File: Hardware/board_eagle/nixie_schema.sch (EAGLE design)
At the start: 116 parts, among them J2 RTC_CONSMD, J4 RTC_CONTHT, P1 100k, P2 10k, Q1 BC856B, Q3 BC856B, Q4 BCX70H, Q5 NTF5P03, T1 PHOTO_TRANS, U2 MC7940N, U3 1V5, Y1 ECS-.327-7-34B

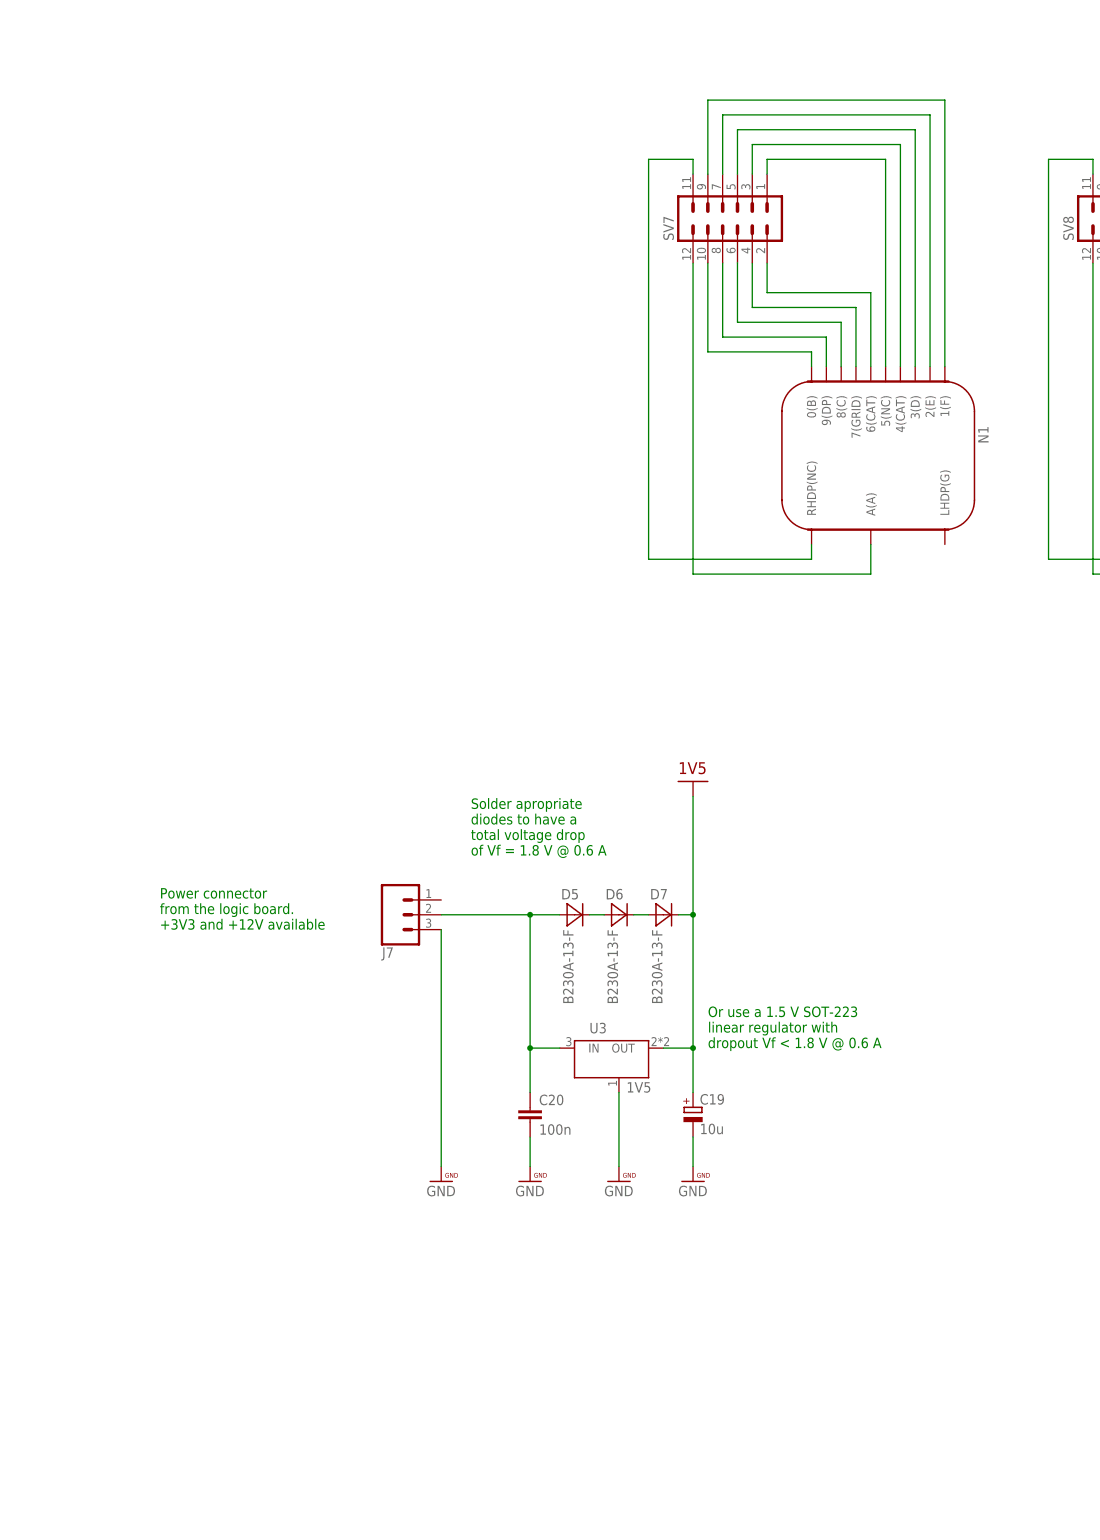
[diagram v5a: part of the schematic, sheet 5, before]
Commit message: Figured out how to wire up tubes to support both IN-14 and IV-11
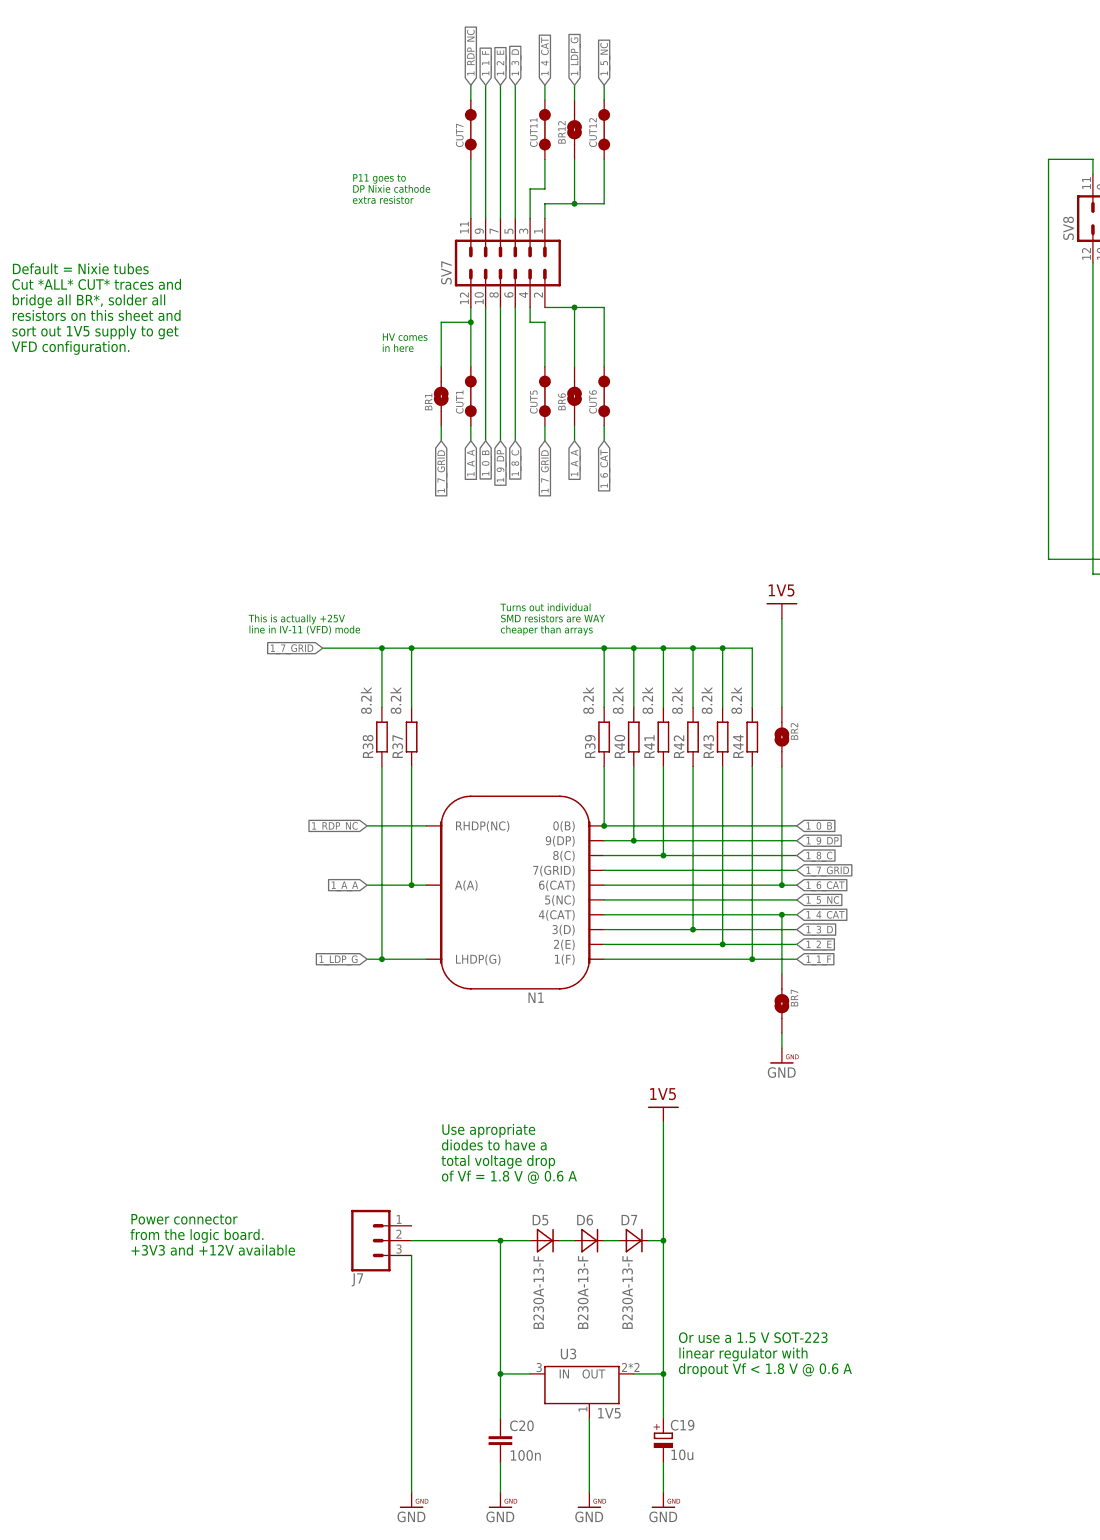
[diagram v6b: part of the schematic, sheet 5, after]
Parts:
- added BR1, BR12, BR2, BR6, BR7: HV_SOLDER_BRIDGE, nixe_cmp:HV_SOLDER_BRIDGE
- added CUT1, CUT11, CUT12, CUT5, CUT6, CUT7: CUT_TRACE, nixe_cmp:CUT_TRACE
- added R37, R38, R39, R40, R41, R42, R43, R44: 8.2k, rcl:R-EU_R0603
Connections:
- removed net N$25: N1.1(F), SV7.9
- removed net N$27: N1.3(D), SV7.5
- removed net N$28: N1.4(CAT), SV7.3
- removed net N$6: N1.7(GRID), SV7.4
- removed net N$7: N1.8(C), SV7.6
- removed net N$94: N1.0(B), SV7.10
- new net 1_0_B: N1.0(B), R39.1, SV7.10
- new net 1_1_F: N1.1(F), R44.1, SV7.9
- new net 1_2_E: N1.2(E), R43.1, SV7.7
- new net 1_3_D: N1.3(D), R42.1, SV7.5
- new net 1_4_CAT: BR7.1, CUT11.2, N1.4(CAT)
- new net 1_5_NC: CUT12.2, N1.5(NC)
- new net 1_6_CAT: CUT6.1, N1.6(CAT)
- new net 1_7_GRID: BR1.1, CUT5.1, N1.7(GRID), R37.2, R38.2, R39.2, R40.2, R41.2, R42.2, R43.2, R44.2
- new net 1_8_C: N1.8(C), R41.1, SV7.6
- new net 1_9_DP: N1.9(DP), R40.1, SV7.8
- new net 1_A_A: BR6.1, CUT1.1, N1.A(A), R37.1
- new net 1_LDP_G: BR12.2, N1.LHDP(G), R38.1
- new net 1_RDP_NC: CUT7.2, N1.RHDP(NC)
- net GND: now also BR7.2
- net N$10: now also BR6.2, CUT6.2, SV7.2; no longer N1.A(A), SV7.12
- net N$2: now also BR1.2, CUT1.2, SV7.12; no longer N1.6(CAT), SV7.2
- net N$24: now also CUT5.2, SV7.4; no longer N1.9(DP), SV7.8
- net N$26: now also CUT7.1, SV7.11; no longer N1.2(E), SV7.7
- net N$29: now also BR12.1, CUT12.1; no longer N1.5(NC)
- net N$30: now also CUT11.1, SV7.3; no longer N1.RHDP(NC), SV7.11
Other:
- note added: "Default = Nixie tubes Cut *ALL* CUT* traces and bridge all BR*, solder all resistors on this sheet and sort out 1V5 supply to get VFD configuration."
- note added: "HV comes in here"
- note added: "P11 goes to DP Nixie cathode extra resistor"
- note added: "This is actually +25V line in IV-11 (VFD) mode"
- note added: "Turns out individual SMD resistors are WAY cheaper than arrays"
- note added: "Use apropriate diodes to have a total voltage drop of Vf = 1.8 V @ 0.6 A"
- note removed: "Solder apropriate diodes to have a total voltage drop of Vf = 1.8 V @ 0.6 A"
- moved on the sheet: C19, C20, D5, D6, D7, J7, N1, SV7, U3

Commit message: Finished tube schematic layout
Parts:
- added BR10, BR11, BR13, BR14, BR15, BR16, BR17, BR18, BR19, BR20, BR21, BR22, BR23, BR24, BR25, BR26, BR27, BR28, BR29, BR3, BR30, BR4, BR5, BR8, BR9: HV_SOLDER_BRIDGE, nixe_cmp:HV_SOLDER_BRIDGE
- added CUT10, CUT13, CUT14, CUT15, CUT16, CUT17, CUT18, CUT19, CUT2, CUT20, CUT21, CUT22, CUT23, CUT24, CUT25, CUT26, CUT27, CUT28, CUT29, CUT3, CUT30, CUT31, CUT32, CUT33, CUT34, CUT35, CUT36, CUT4, CUT8, CUT9: CUT_TRACE, nixe_cmp:CUT_TRACE
- added R45, R46, R47, R48, R49, R50, R51, R52, R53, R54, R55, R56, R57, R58, R59, R60, R61, R62, R63, R64, R65, R66, R67, R68, R69, R70, R71, R72, R73, R74, R75, R76, R77, R78, R79, R80, R81, R82, R83, R84: 8.2k, rcl:R-EU_R0603
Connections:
- removed net N$52: N3.2(E), SV9.7
- removed net N$53: N3.1(F), SV9.9
- removed net N$54: N4.7(GRID), SV10.4
- removed net N$55: N4.8(C), SV10.6
- removed net N$56: N4.9(DP), SV10.8
- removed net N$57: N4.0(B), SV10.10
- removed net N$58: N5.RHDP(NC), SV11.11
- removed net N$59: N4.5(NC), SV10.1
- removed net N$60: N4.4(CAT), SV10.3
- removed net N$61: N4.3(D), SV10.5
- removed net N$62: N4.2(E), SV10.7
- removed net N$63: N4.1(F), SV10.9
- removed net N$64: N5.6(CAT), SV11.2
- removed net N$65: N5.7(GRID), SV11.4
- removed net N$66: N5.8(C), SV11.6
- removed net N$67: N5.9(DP), SV11.8
- removed net N$68: N5.0(B), SV11.10
- removed net N$69: N5.5(NC), SV11.1
- removed net N$70: N5.4(CAT), SV11.3
- removed net N$71: N5.3(D), SV11.5
- removed net N$72: N5.2(E), SV11.7
- removed net N$73: N5.1(F), SV11.9
- removed net N$75: N6.RHDP(NC), SV12.11
- removed net N$76: N6.6(CAT), SV12.2
- removed net N$77: N6.7(GRID), SV12.4
- removed net N$78: N6.8(C), SV12.6
- removed net N$79: N6.9(DP), SV12.8
- removed net N$80: N6.5(NC), SV12.1
- removed net N$81: N6.4(CAT), SV12.3
- removed net N$82: N6.3(D), SV12.5
- removed net N$83: N6.2(E), SV12.7
- removed net N$84: N6.1(F), SV12.9
- removed net N$86: N6.0(B), SV12.10
- removed net N$88: N4.A(A), SV10.12
- removed net N$98: N5.A(A), SV11.12
- new net 2_0_B: N2.0(B), R47.1, SV8.10
- new net 2_1_F: N2.1(F), R52.1, SV8.9
- new net 2_2_E: N2.2(E), R51.1, SV8.7
- new net 2_3_D: N2.3(D), R50.1, SV8.5
- new net 2_4_CAT: BR3.1, CUT9.2, N2.4(CAT)
- new net 2_5_NC: CUT10.2, N2.5(NC)
- new net 2_6_CAT: BR4.2, CUT4.1, N2.6(CAT)
- new net 2_7_GRID: BR5.1, CUT3.1, N2.7(GRID), R45.2, R46.2, R47.2, R48.2, R49.2, R50.2, R51.2, R52.2
- new net 2_8_C: N2.8(C), R49.1, SV8.6
- new net 2_9_DP: N2.9(DP), R48.1, SV8.8
- new net 2_A_A: BR8.1, CUT2.1, N2.A(A), R45.1
- new net 2_LDP_G: BR9.2, N2.LHDP(G), R46.1
- new net 2_RDP_NC: CUT8.2, N2.RHDP(NC)
- new net 3_0_B: N3.0(B), R55.1, SV9.10
- new net 3_1_F: N3.1(F), R60.1, SV9.9
- new net 3_2_E: N3.2(E), R59.1, SV9.7
- new net 3_3_D: N3.3(D), R58.1, SV9.5
- new net 3_4_CAT: BR10.1, CUT17.2, N3.4(CAT)
- new net 3_5_NC: CUT18.2, N3.5(NC)
- new net 3_6_CAT: BR11.2, CUT15.1, N3.6(CAT)
- new net 3_7_GRID: BR13.1, CUT14.1, N3.7(GRID), R53.2, R54.2, R55.2, R56.2, R57.2, R58.2, R59.2, R60.2
- new net 3_8_C: N3.8(C), R57.1, SV9.6
- new net 3_9_DP: N3.9(DP), R56.1, SV9.8
- new net 3_A_A: BR14.1, CUT13.1, N3.A(A), R53.1
- new net 3_LDP_G: BR15.2, N3.LHDP(G), R54.1
- new net 3_RDP_NC: CUT16.2, N3.RHDP(NC)
- new net 4_0_B: N4.0(B), R63.1, SV10.10
- new net 4_1_F: N4.1(F), R68.1, SV10.9
- new net 4_2_E: N4.2(E), R67.1, SV10.7
- new net 4_3_D: N4.3(D), R66.1, SV10.5
- new net 4_4_CAT: BR19.1, CUT23.2, N4.4(CAT)
- new net 4_5_NC: CUT24.2, N4.5(NC)
- new net 4_6_CAT: BR20.2, CUT21.1, N4.6(CAT)
- new net 4_7_GRID: BR16.1, CUT20.1, N4.7(GRID), R61.2, R62.2, R63.2, R64.2, R65.2, R66.2, R67.2, R68.2
- new net 4_8_C: N4.8(C), R65.1, SV10.6
- new net 4_9_DP: N4.9(DP), R64.1, SV10.8
- new net 4_A_A: BR17.1, CUT19.1, N4.A(A), R61.1
- new net 4_LDP_G: BR18.2, N4.LHDP(G), R62.1
- new net 4_RDP_NC: CUT22.2, N4.RHDP(NC)
- new net 5_0_B: N5.0(B), R71.1, SV11.10
- new net 5_1_F: N5.1(F), R76.1, SV11.9
- new net 5_2_E: N5.2(E), R75.1, SV11.7
- new net 5_3_D: N5.3(D), R74.1, SV11.5
- new net 5_4_CAT: BR21.1, CUT29.2, N5.4(CAT)
- new net 5_5_NC: CUT30.2, N5.5(NC)
- new net 5_6_CAT: BR22.2, CUT27.1, N5.6(CAT)
- new net 5_7_GRID: BR23.1, CUT26.1, N5.7(GRID), R69.2, R70.2, R71.2, R72.2, R73.2, R74.2, R75.2, R76.2
- new net 5_8_C: N5.8(C), R73.1, SV11.6
- new net 5_9_DP: N5.9(DP), R72.1, SV11.8
- new net 5_A_A: BR24.1, CUT25.1, N5.A(A), R69.1
- new net 5_LDP_G: BR25.2, N5.LHDP(G), R70.1
- new net 5_RDP_NC: CUT28.2, N5.RHDP(NC)
- new net 6_0_B: N6.0(B), R79.1, SV12.10
- new net 6_1_F: N6.1(F), R84.1, SV12.9
- new net 6_2_E: N6.2(E), R83.1, SV12.7
- new net 6_3_D: N6.3(D), R82.1, SV12.5
- new net 6_4_CAT: BR26.1, CUT35.2, N6.4(CAT)
- new net 6_5_NC: CUT36.2, N6.5(NC)
- new net 6_6_CAT: BR27.2, CUT33.1, N6.6(CAT)
- new net 6_7_GRID: BR28.1, CUT32.1, N6.7(GRID), R77.2, R78.2, R79.2, R80.2, R81.2, R82.2, R83.2, R84.2
- new net 6_8_C: N6.8(C), R81.1, SV12.6
- new net 6_9_DP: N6.9(DP), R80.1, SV12.8
- new net 6_A_A: BR29.1, CUT31.1, N6.A(A), R77.1
- new net 6_LDP_G: BR30.2, N6.LHDP(G), R78.1
- new net 6_RDP_NC: CUT34.2, N6.RHDP(NC)
- new net N$25: CUT9.1, SV8.3
- new net N$27: BR14.2, CUT15.2, SV9.2
- new net N$28: CUT14.2, SV9.4
- new net N$6: BR8.2, CUT4.2, SV8.2
- new net N$7: CUT3.2, SV8.4
- net 1V5: now also BR11.1, BR2.1, BR20.1, BR22.1, BR27.1, BR4.1
- net 1_6_CAT: now also BR2.2
- net GND: now also BR10.2, BR19.2, BR21.2, BR26.2, BR3.2
- net N$1: now also BR5.2, CUT2.2, SV8.12; no longer N2.RHDP(NC), SV8.11
- net N$19: now also CUT8.1, SV8.11; no longer N2.A(A), SV8.12
- net N$21: now also BR13.2, CUT13.2; no longer N3.A(A)
- net N$23: now also BR9.1, CUT10.1, SV8.1; no longer N2.6(CAT), SV8.2
- net N$31: now also CUT16.1, SV9.11; no longer N2.7(GRID), SV8.4
- net N$32: now also BR15.1, CUT18.1, SV9.1; no longer N2.8(C), SV8.6
- net N$33: now also CUT17.1, SV9.3; no longer N2.9(DP), SV8.8
- net N$34: now also BR16.2, CUT19.2, SV10.12; no longer N2.0(B), SV8.10
- net N$35: now also BR17.2, CUT21.2, SV10.2; no longer N3.RHDP(NC), SV9.11
- net N$36: now also CUT20.2, SV10.4; no longer N3.6(CAT), SV9.2
- net N$37: now also CUT22.1, SV10.11; no longer N3.7(GRID), SV9.4
- net N$38: now also BR18.1, CUT24.1, SV10.1; no longer N2.5(NC), SV8.1
- net N$39: now also CUT23.1, SV10.3; no longer N2.4(CAT), SV8.3
- net N$40: now also BR23.2, CUT25.2, SV11.12; no longer N2.3(D), SV8.5
- net N$41: now also BR24.2, CUT27.2, SV11.2; no longer N2.2(E), SV8.7
- net N$42: now also CUT26.2, SV11.4; no longer N2.1(F), SV8.9
- net N$43: now also CUT28.1, SV11.11; no longer N3.8(C), SV9.6
- net N$44: now also BR25.1, CUT30.1, SV11.1; no longer N3.9(DP), SV9.8
- net N$45: now also BR28.2, CUT31.2; no longer N6.A(A)
- net N$46: now also CUT29.1, SV11.3; no longer N3.0(B), SV9.10
- net N$47: now also BR29.2, CUT33.2, SV12.2; no longer N4.RHDP(NC), SV10.11
- net N$48: now also CUT32.2, SV12.4; no longer N4.6(CAT), SV10.2
- net N$49: now also CUT34.1, SV12.11; no longer N3.5(NC), SV9.1
- net N$50: now also BR30.1, CUT36.1, SV12.1; no longer N3.4(CAT), SV9.3
- net N$51: now also CUT35.1, SV12.3; no longer N3.3(D), SV9.5
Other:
- moved on the sheet: BR1, BR12, BR2, BR6, BR7, C19, C20, CUT1, CUT11, CUT12, CUT5, CUT6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

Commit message: Some initial experimental routing for the top board
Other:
- moved on the sheet: BR1, BR10, BR11, BR12, BR13, BR14, BR15, BR16, BR17, BR18, BR19, BR2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
